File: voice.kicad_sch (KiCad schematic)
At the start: 43 parts, among them J14 Conn_01x02, J15 Conn_01x02, SW1 SW_Wuerth_450301014042, U1 WM8960CGEFL_V, U2 AP2112K-3.3, Y1 ECS-3225MV

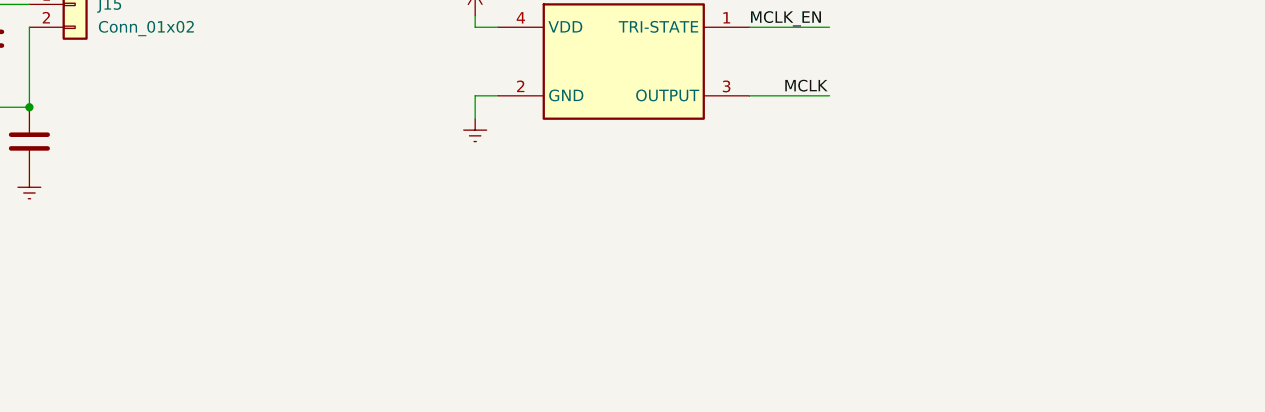
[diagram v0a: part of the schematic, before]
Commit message: added reference to the voice sch
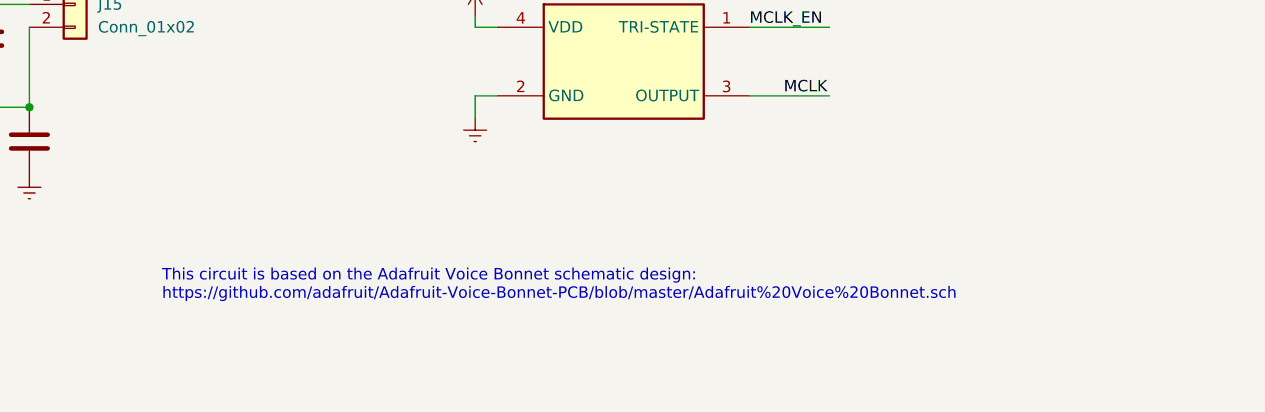
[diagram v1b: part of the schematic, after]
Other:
- note added: "This circuit is based on the Adafruit Voice Bonnet schematic design: https://github.com/adafruit/Adafruit-Voice-Bonnet-PCB/blob/master/Adafruit%20Voice%20Bonnet.sch"
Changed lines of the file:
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@@
 	(title_block
 		(title "RSC hat board")
-		(date "2026-04-30")
+		(date "2026-05-18")
 		(rev "A")
 		(comment 1 "Author: Raiko Torga")
 	)
+	(text "This circuit is based on the Adafruit Voice Bonnet schematic design:\nhttps://github.com/adafruit/Adafruit-Voice-Bonnet-PCB/blob/master/Adafruit%20Voice%20Bonnet.sch\n"
+		(exclude_from_sim no)
+		(at 177.292 168.402 0)
+		(effects
+			(font
+				(size 1.27 1.27)
+			)
+			(justify left)
+		)
+	)
 	(junction
